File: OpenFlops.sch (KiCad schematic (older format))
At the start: 74 parts, among them P1 FLOPPY_CONN, P2 POWER_INPUT, P3 USB_A_FEMALE, P4 PROG_PORT, P5 JUMPERS, P6 ENCODER_PORT, P7 DISPLAY_PORT, Q1 MOS_N_GSD, Q2 MOS_N_GSD, Q3 MOS_N_GSD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

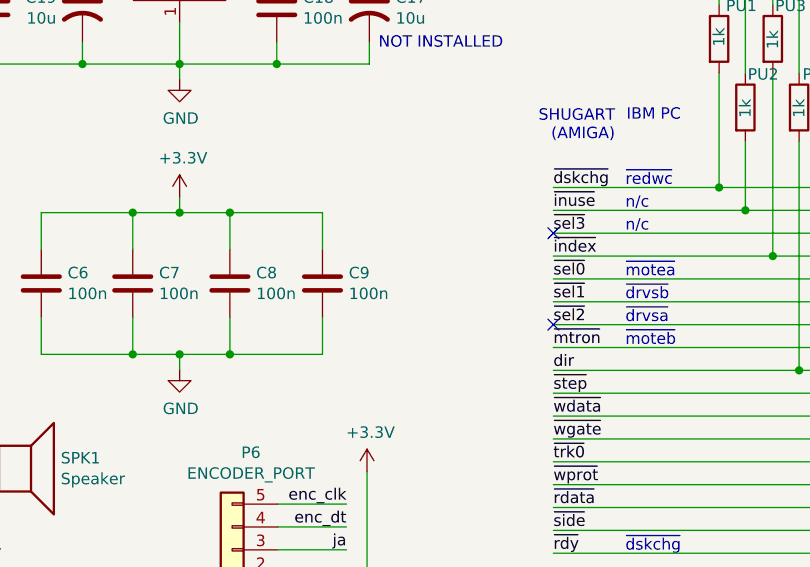
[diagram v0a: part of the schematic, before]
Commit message: Rework power tracks, depolarize OLED/encoder connectors
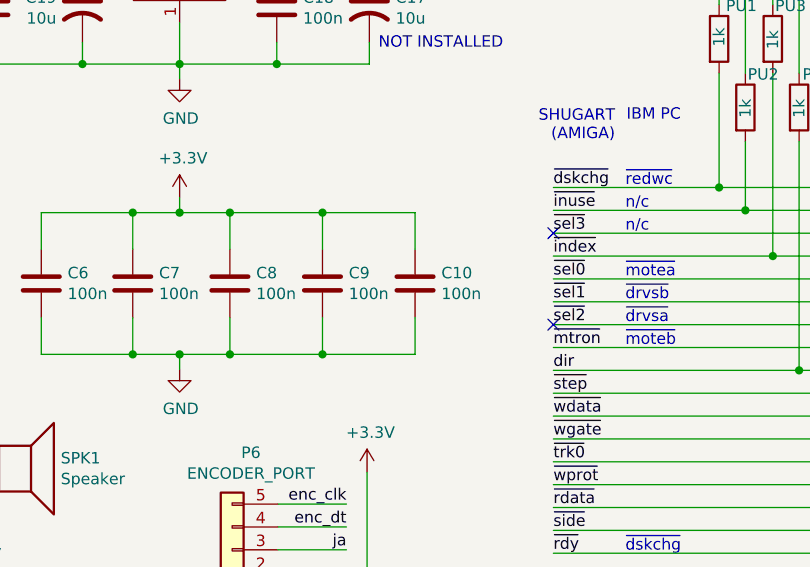
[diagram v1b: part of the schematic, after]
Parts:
- added C10: 100n, Capacitor_SMD:C_0805_2012Metric_Pad1.15x1.40mm_HandSolder, symbol Device:C
- P6: footprint Connector_PinHeader_2.54mm:PinHeader_1x05_P2.54mm_Vertical -> OpenFlops:PinHeader_1x05_P2.54mm_Vertical
- P7: footprint Connector_PinHeader_2.54mm:PinHeader_1x04_P2.54mm_Vertical -> OpenFlops:PinHeader_1x04_P2.54mm_Vertical
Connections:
- net +3V3: now also C10.1
- net GND: now also C10.2
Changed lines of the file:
@@
 Sheet 1 1
 Title "OpenFlops"
-Date "2019-08-04"
+Date "2019-08-14"
 Rev "1git"
 Comp "SukkoPera"
@@
 F 0 "P7" H 7553 4925 50  0000 C CNN
 F 1 "DISPLAY_PORT" H 7553 5016 50  0000 C CNN
-F 2 "Connector_PinHeader_2.54mm:PinHeader_1x04_P2.54mm_Vertical" H 7635 5350 50  0001 C CNN
+F 2 "OpenFlops:PinHeader_1x04_P2.54mm_Vertical" H 7635 5350 50  0001 C CNN
 F 3 "~" H 7635 5350 50  0001 C CNN
 	1    7635 5350
@@
 F 0 "P6" H 6018 4165 50  0000 C CNN
 F 1 "ENCODER_PORT" H 6018 4256 50  0000 C CNN
-F 2 "Connector_PinHeader_2.54mm:PinHeader_1x05_P2.54mm_Vertical" H 6100 4590 50  0001 C CNN
+F 2 "OpenFlops:PinHeader_1x05_P2.54mm_Vertical" H 6100 4590 50  0001 C CNN
 F 3 "~" H 6100 4590 50  0001 C CNN
 	1    6100 4590
@@
 Wire Wire Line
 	4905 4435 4905 4455
+$Comp
+L Device:C C10
+U 1 1 5D58F4BB
+P 6900 3425
+F 0 "C10" H 7015 3471 50  0000 L CNN
+F 1 "100n" H 7015 3380 50  0000 L CNN
+F 2 "Capacitor_SMD:C_0805_2012Metric_Pad1.15x1.40mm_HandSolder" H 6938 3275 50  0001 C CNN
+F 3 "~" H 6900 3425 50  0001 C CNN
+	1    6900 3425
+	1    0    0    -1
+$EndComp
+Wire Wire Line
+	6900 3115 6900 3275
+Wire Wire Line
+	6495 3115 6900 3115
+Wire Wire Line
+	6495 3735 6900 3735
+Wire Wire Line
+	6900 3735 6900 3575
+Connection ~ 6495 3115
+Connection ~ 6495 3735
 $EndSCHEMATC

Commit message: Use SOT-23 footprints for MOSFETs
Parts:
- Q1, Q2, Q3, Q4, Q5, Q6: footprint Package_TO_SOT_SMD:SOT-323_SC-70_Handsoldering -> Package_TO_SOT_SMD:SOT-23_Handsoldering
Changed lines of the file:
@@
 F 0 "Q1" H 3216 5643 70  0000 L CNN
 F 1 "MOS_N_GSD" H 3216 5529 60  0000 L CNN
-F 2 "Package_TO_SOT_SMD:SOT-323_SC-70_Handsoldering" H 3040 5590 60  0001 C CNN
+F 2 "Package_TO_SOT_SMD:SOT-23_Handsoldering" H 3040 5590 60  0001 C CNN
 F 3 "" H 3040 5590 60  0000 C CNN
 	1    3040 5590
@@
 F 0 "Q2" H 3216 6493 70  0000 L CNN
 F 1 "MOS_N_GSD" H 3216 6379 60  0000 L CNN
-F 2 "Package_TO_SOT_SMD:SOT-323_SC-70_Handsoldering" H 3040 6440 60  0001 C CNN
+F 2 "Package_TO_SOT_SMD:SOT-23_Handsoldering" H 3040 6440 60  0001 C CNN
 F 3 "" H 3040 6440 60  0000 C CNN
 	1    3040 6440
@@
 F 0 "Q3" H 3216 7343 70  0000 L CNN
 F 1 "MOS_N_GSD" H 3216 7229 60  0000 L CNN
-F 2 "Package_TO_SOT_SMD:SOT-323_SC-70_Handsoldering" H 3040 7290 60  0001 C CNN
+F 2 "Package_TO_SOT_SMD:SOT-23_Handsoldering" H 3040 7290 60  0001 C CNN
 F 3 "" H 3040 7290 60  0000 C CNN
 	1    3040 7290
@@
 F 0 "Q6" H 5876 7343 70  0000 L CNN
 F 1 "MOS_N_GSD" H 5876 7229 60  0000 L CNN
-F 2 "Package_TO_SOT_SMD:SOT-323_SC-70_Handsoldering" H 5700 7290 60  0001 C CNN
+F 2 "Package_TO_SOT_SMD:SOT-23_Handsoldering" H 5700 7290 60  0001 C CNN
 F 3 "" H 5700 7290 60  0000 C CNN
 	1    5700 7290
@@
 F 0 "Q5" H 5876 6493 70  0000 L CNN
 F 1 "MOS_N_GSD" H 5876 6379 60  0000 L CNN
-F 2 "Package_TO_SOT_SMD:SOT-323_SC-70_Handsoldering" H 5700 6440 60  0001 C CNN
+F 2 "Package_TO_SOT_SMD:SOT-23_Handsoldering" H 5700 6440 60  0001 C CNN
 F 3 "" H 5700 6440 60  0000 C CNN
 	1    5700 6440
@@
 F 0 "Q4" H 5876 5643 70  0000 L CNN
 F 1 "MOS_N_GSD" H 5876 5529 60  0000 L CNN
-F 2 "Package_TO_SOT_SMD:SOT-323_SC-70_Handsoldering" H 5700 5590 60  0001 C CNN
+F 2 "Package_TO_SOT_SMD:SOT-23_Handsoldering" H 5700 5590 60  0001 C CNN
 F 3 "" H 5700 5590 60  0000 C CNN
 	1    5700 5590

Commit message: Use SOD-323 footprint for diodes
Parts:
- D1, D2: footprint Diode_SMD:D_SOD-123 -> Diode_SMD:D_SOD-323_HandSoldering
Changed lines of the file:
@@
 F 0 "D1" H 5375 6561 50  0000 C CNN
 F 1 "1N5819 (?)" H 5375 6470 50  0000 C CNN
-F 2 "Diode_SMD:D_SOD-123" H 5375 6685 50  0001 C CNN
+F 2 "Diode_SMD:D_SOD-323_HandSoldering" H 5375 6685 50  0001 C CNN
 F 3 "~" H 5375 6685 50  0001 C CNN
 	1    5375 6685
@@
 F 0 "D2" V 4674 4324 50  0000 L CNN
 F 1 "1N5819 (?)" V 4765 4324 50  0000 L CNN
-F 2 "Diode_SMD:D_SOD-123" H 4720 4245 50  0001 C CNN
+F 2 "Diode_SMD:D_SOD-323_HandSoldering" H 4720 4245 50  0001 C CNN
 F 3 "~" H 4720 4245 50  0001 C CNN
 	1    4720 4245

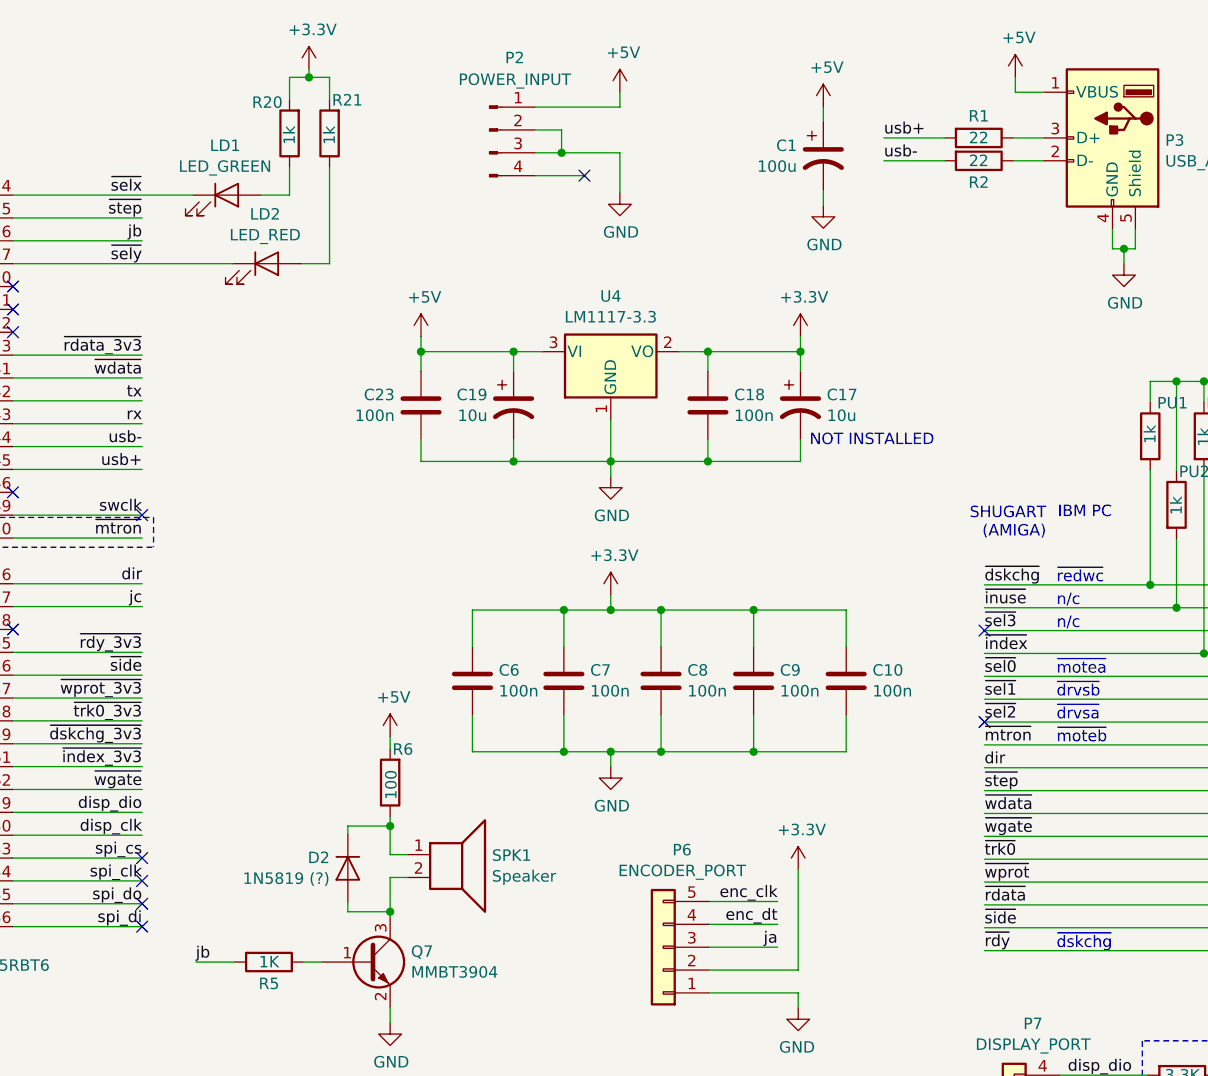
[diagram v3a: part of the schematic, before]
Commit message: Add header for USB and speaker signals - Thanks Ray Bellis
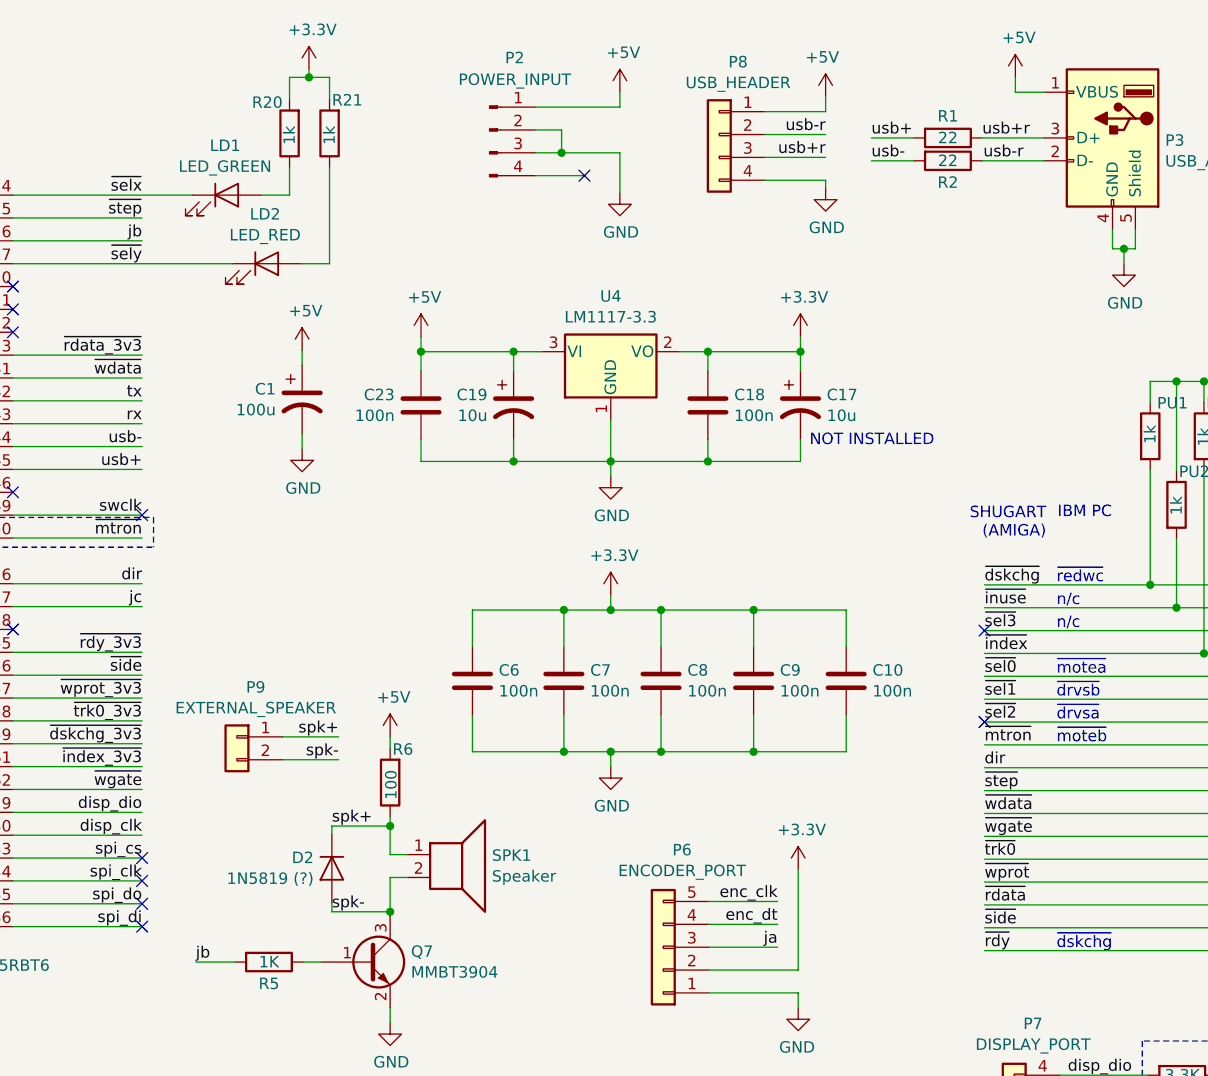
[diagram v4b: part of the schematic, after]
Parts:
- added P8: USB_HEADER, OpenFlops:PinHeader_1x04_P2.54mm_Vertical, symbol Connector_Generic:Conn_01x04
- added P9: EXTERNAL_SPEAKER, OpenFlops:PinHeader_1x02_P2.54mm_Vertical, symbol Connector_Generic:Conn_01x02
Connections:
- net +5V: now also P8.1 (Pin_1)
- net GND: now also P8.4 (Pin_4)
- net spk+: now reaches D2.1 (K), R6.1, SPK1.1
- net spk+: now also P9.1 (Pin_1)
- net spk-: now reaches D2.2 (A), Q7.3 (C), SPK1.2
- net spk-: now also P9.2 (Pin_2)
- net usb-r: now reaches P3.2 (D-), R2.1
- net usb-r: now also P8.2 (Pin_2)
- net usb+r: now reaches P3.3 (D+), R1.1
- net usb+r: now also P8.3 (Pin_3)
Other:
- moved on the sheet: C1, D2, R1, R2
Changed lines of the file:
@@
 Sheet 1 1
 Title "OpenFlops"
-Date "2019-08-14"
+Date "2019-08-18"
 Rev "1git"
 Comp "SukkoPera"
@@
 L Device:R R1
 U 1 1 5D7861B9
-P 7480 1050
-F 0 "R1" V 7385 1050 50  0000 C CNN
-F 1 "22" V 7480 1050 50  0000 C CNN
-F 2 "Resistor_SMD:R_0805_2012Metric_Pad1.15x1.40mm_HandSolder" V 7410 1050 50  0001 C CNN
-F 3 "~" H 7480 1050 50  0001 C CNN
-	1    7480 1050
+P 7345 1050
+F 0 "R1" V 7250 1050 50  0000 C CNN
+F 1 "22" V 7345 1050 50  0000 C CNN
+F 2 "Resistor_SMD:R_0805_2012Metric_Pad1.15x1.40mm_HandSolder" V 7275 1050 50  0001 C CNN
+F 3 "~" H 7345 1050 50  0001 C CNN
+	1    7345 1050
 	0    1    1    0
 $EndComp
@@
 L Device:R R2
 U 1 1 5D786893
-P 7480 1150
-F 0 "R2" V 7575 1150 50  0000 C CNN
-F 1 "22" V 7480 1150 50  0000 C CNN
-F 2 "Resistor_SMD:R_0805_2012Metric_Pad1.15x1.40mm_HandSolder" V 7410 1150 50  0001 C CNN
-F 3 "~" H 7480 1150 50  0001 C CNN
-	1    7480 1150
+P 7345 1150
+F 0 "R2" V 7440 1150 50  0000 C CNN
+F 1 "22" V 7345 1150 50  0000 C CNN
+F 2 "Resistor_SMD:R_0805_2012Metric_Pad1.15x1.40mm_HandSolder" V 7275 1150 50  0001 C CNN
+F 3 "~" H 7345 1150 50  0001 C CNN
+	1    7345 1150
 	0    1    1    0
 $EndComp
 Wire Wire Line
-	7630 1050 7765 1050
-Wire Wire Line
-	7630 1150 7765 1150
-Wire Wire Line
-	7330 1050 7065 1050
-Wire Wire Line
-	7330 1150 7065 1150
-Text Label 7065 1050 0    50   ~ 0
+	7495 1050 7765 1050
+Wire Wire Line
+	7195 1050 7010 1050
+Wire Wire Line
+	7195 1150 7010 1150
+Text Label 7010 1050 0    50   ~ 0
 usb+
-Text Label 7065 1150 0    50   ~ 0
+Text Label 7010 1150 0    50   ~ 0
 usb-
 Wire Wire Line
@@
 L Device:CP1 C1
 U 1 1 5EE6C285
-P 6800 1130
-F 0 "C1" H 6685 1176 50  0000 R CNN
-F 1 "100u" H 6685 1085 50  0000 R CNN
-F 2 "Capacitor_THT:CP_Radial_D6.3mm_P2.50mm" H 6800 1130 50  0001 C CNN
-F 3 "~" H 6800 1130 50  0001 C CNN
-	1    6800 1130
+P 4520 2195
+F 0 "C1" H 4405 2241 50  0000 R CNN
+F 1 "100u" H 4405 2150 50  0000 R CNN
+F 2 "Capacitor_THT:CP_Radial_D6.3mm_P2.50mm" H 4520 2195 50  0001 C CNN
+F 3 "~" H 4520 2195 50  0001 C CNN
+	1    4520 2195
 	1    0    0    -1
 $EndComp
@@
 L power:+5V #PWR0141
 U 1 1 5EE997A6
-P 6800 915
-F 0 "#PWR0141" H 6800 765 50  0001 C CNN
-F 1 "+5V" H 6815 1088 50  0000 C CNN
-F 2 "" H 6800 915 50  0001 C CNN
-F 3 "" H 6800 915 50  0001 C CNN
-	1    6800 915
-	1    0    0    -1
-$EndComp
-Wire Wire Line
-	6800 915  6800 980
+P 4520 1980
+F 0 "#PWR0141" H 4520 1830 50  0001 C CNN
+F 1 "+5V" H 4535 2153 50  0000 C CNN
+F 2 "" H 4520 1980 50  0001 C CNN
+F 3 "" H 4520 1980 50  0001 C CNN
+	1    4520 1980
+	1    0    0    -1
+$EndComp
+Wire Wire Line
+	4520 1980 4520 2045
 $Comp
 L power:GND #PWR0142
 U 1 1 5EEC2A25
-P 6800 1345
-F 0 "#PWR0142" H 6800 1095 50  0001 C CNN
-F 1 "GND" H 6805 1172 50  0000 C CNN
-F 2 "" H 6800 1345 50  0001 C CNN
-F 3 "" H 6800 1345 50  0001 C CNN
-	1    6800 1345
-	1    0    0    -1
-$EndComp
-Wire Wire Line
-	6800 1280 6800 1345
+P 4520 2410
+F 0 "#PWR0142" H 4520 2160 50  0001 C CNN
+F 1 "GND" H 4525 2237 50  0000 C CNN
+F 2 "" H 4520 2410 50  0001 C CNN
+F 3 "" H 4520 2410 50  0001 C CNN
+	1    4520 2410
+	1    0    0    -1
+$EndComp
+Wire Wire Line
+	4520 2345 4520 2410
 Text Label 7505 3305 0    50   ~ 0
 ~index
@@
 	4905 4020 4905 4060
 Wire Wire Line
-	4720 4095 4720 4060
-Wire Wire Line
-	4720 4060 4905 4060
+	4650 4095 4650 4060
+Wire Wire Line
+	4650 4060 4905 4060
 Connection ~ 4905 4060
 Wire Wire Line
 	4905 4060 4905 4185
-Wire Wire Line
-	4720 4395 4720 4435
 $Comp
 L Device:D D2
 U 1 1 5E2F4A52
-P 4720 4245
-F 0 "D2" V 4674 4324 50  0000 L CNN
-F 1 "1N5819 (?)" V 4765 4324 50  0000 L CNN
-F 2 "Diode_SMD:D_SOD-323_HandSoldering" H 4720 4245 50  0001 C CNN
-F 3 "~" H 4720 4245 50  0001 C CNN
-	1    4720 4245
+P 4650 4245
+F 0 "D2" V 4604 4324 50  0000 L CNN
+F 1 "1N5819 (?)" V 4695 4324 50  0000 L CNN
+F 2 "Diode_SMD:D_SOD-323_HandSoldering" H 4650 4245 50  0001 C CNN
+F 3 "~" H 4650 4245 50  0001 C CNN
+	1    4650 4245
 	0    -1   1    0
 $EndComp
@@
 Wire Wire Line
 	4905 4285 4905 4435
-Wire Wire Line
-	4720 4435 4905 4435
 Connection ~ 4905 4435
 Wire Wire Line
@@
 Connection ~ 6495 3115
 Connection ~ 6495 3735
+$Comp
+L Connector_Generic:Conn_01x04 P8
+U 1 1 5D653966
+P 6345 1035
+F 0 "P8" H 6263 1352 50  0000 C CNN
+F 1 "USB_HEADER" H 6263 1261 50  0000 C CNN
+F 2 "OpenFlops:PinHeader_1x04_P2.54mm_Vertical" H 6345 1035 50  0001 C CNN
+F 3 "~" H 6345 1035 50  0001 C CNN
+	1    6345 1035
+	-1   0    0    -1
+$EndComp
+Wire Wire Line
+	6545 1035 6810 1035
+Wire Wire Line
+	6545 1135 6810 1135
+Text Label 6810 1035 2    50   ~ 0
+usb-r
+Text Label 6810 1135 2    50   ~ 0
+usb+r
+$Comp
+L power:+5V #PWR0144
+U 1 1 5D74D3BF
+P 6810 870
+F 0 "#PWR0144" H 6810 720 50  0001 C CNN
+F 1 "+5V" H 6825 1043 50  0000 C CNN
+F 2 "" H 6810 870 50  0001 C CNN
+F 3 "" H 6810 870 50  0001 C CNN
+	1    6810 870
+	-1   0    0    -1
+$EndComp
+Wire Wire Line
+	6810 870  6810 935
+Wire Wire Line
+	6810 935  6545 935
+$Comp
+L power:GND #PWR0145
+U 1 1 5D780CD9
+P 6810 1270
+F 0 "#PWR0145" H 6810 1020 50  0001 C CNN
+F 1 "GND" H 6815 1097 50  0000 C CNN
+F 2 "" H 6810 1270 50  0001 C CNN
+F 3 "" H 6810 1270 50  0001 C CNN
+	1    6810 1270
+	1    0    0    -1
+$EndComp
+Wire Wire Line
+	6545 1235 6810 1235
+Wire Wire Line
+	6810 1235 6810 1270
+$Comp
+L Connector_Generic:Conn_01x02 P9
+U 1 1 5D86073A
+P 4235 3670
+F 0 "P9" H 4153 3887 50  0000 C CNN
+F 1 "EXTERNAL_SPEAKER" H 4153 3796 50  0000 C CNN
+F 2 "OpenFlops:PinHeader_1x02_P2.54mm_Vertical" H 4235 3670 50  0001 C CNN
+F 3 "~" H 4235 3670 50  0001 C CNN
+	1    4235 3670
+	-1   0    0    -1
+$EndComp
+Wire Wire Line
+	4435 3670 4680 3670
+Wire Wire Line
+	4435 3770 4680 3770
+Wire Wire Line
+	4650 4435 4650 4395
+Wire Wire Line
+	4650 4435 4905 4435
+Text Label 4650 4435 0    50   ~ 0
+spk-
+Text Label 4680 3770 2    50   ~ 0
+spk-
+Text Label 4650 4060 0    50   ~ 0
+spk+
+Text Label 4680 3670 2    50   ~ 0
+spk+
+Text Label 7495 1050 0    50   ~ 0
+usb+r
+Text Label 7500 1150 0    50   ~ 0
+usb-r
+Wire Wire Line
+	7495 1150 7765 1150
 $EndSCHEMATC

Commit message: Lotsa cosmetic fixes
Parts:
- removed P5: JUMPERS, Connector_PinHeader_2.54mm:PinHeader_2x07_P2.54mm_Vertical, symbol Connector_Generic:Conn_02x07_Odd_Even
- added P5: JUMPERS, OpenFlops:PinHeader_1x02_P2.54mm_Vertical, symbol Connector_Generic:Conn_01x02
- added PA5, PB5, PC5, PD5: Conn_01x03, OpenFlops:PinHeader_1x03_P2.54mm_Mute, symbol Connector_Generic:Conn_01x03
- P2: footprint Connector_PinHeader_2.54mm:PinHeader_1x04_P2.54mm_Horizontal -> OpenFlops:PinHeader_1x04_P2.54mm_Vertical
- P4: footprint Connector_PinHeader_2.54mm:PinHeader_2x05_P2.54mm_Vertical -> OpenFlops:PinHeader_2x05_P2.54mm_Vertical
- P9: footprint OpenFlops:PinHeader_1x02_P2.54mm_Vertical -> OpenFlops:PinHeader_1x02_P2.54mm_Mute
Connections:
- net +5V: now also PU15.2, PU4.2; no longer PU15.1, PU4.1
- net GND: now also P5.2 (Pin_2)
- net jc: now also P5.1 (Pin_1)
- net ~mtron: now also PD5.2 (Pin_2)
- net ~sel0: now also PA5.2 (Pin_2)
- net ~sel1: now also PB5.2 (Pin_2)
- net ~sel2: now also PC5.2 (Pin_2)
- net ~selx: now also PU4.1, PA5.1 (Pin_1), PB5.1 (Pin_1), PC5.1 (Pin_1), PD5.1 (Pin_1); no longer PU4.2
- net ~sely: now also PU15.1, PA5.3 (Pin_3), PB5.3 (Pin_3), PC5.3 (Pin_3), PD5.3 (Pin_3); no longer PU15.2
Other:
- note removed: "DRV1 - S0"
- note removed: "DRV1 - S1"
- note removed: "DRV2 - S0"
- note removed: "DRV2 - S1"
- note removed: "J5"
- note removed: "JC"
- note removed: "M0"
- moved on the sheet: LD1, LD2, R20, R21

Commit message: Make LQFP-64 footprint easier to handsolder
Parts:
- U3: footprint Package_QFP:LQFP-64_10x10mm_P0.5mm -> OpenFlops:LQFP-64_Handsoldering
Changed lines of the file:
@@
 F 0 "U3" H 3100 4655 50  0000 C CNN
 F 1 "STM32F105RBT6" H 3125 1130 50  0000 C CNN
-F 2 "Package_QFP:LQFP-64_10x10mm_P0.5mm" H 1955 1200 50  0001 R CNN
+F 2 "OpenFlops:LQFP-64_Handsoldering" H 1955 1200 50  0001 R CNN
 F 3 "http://www.st.com/st-web-ui/static/active/en/resource/technical/document/datasheet/CD00220364.pdf" H 2555 2900 50  0001 C CNN
 	1    2555 2900

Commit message: Ready for V1!
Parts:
- added J99: OSHW_LOGO, Symbol:OSHW-Logo2_9.8x8mm_Copper, symbol Connector_Generic:Conn_01x01
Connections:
- no-connect marks 21 -> 22
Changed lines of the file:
@@
 Sheet 1 1
 Title "OpenFlops"
-Date "2019-08-18"
+Date "2019-08-21"
 Rev "1git"
 Comp "SukkoPera"
@@
 Wire Wire Line
 	3965 785  4045 785
+NoConn ~ 10820 6345
+$Comp
+L Connector_Generic:Conn_01x01 J99
+U 1 1 5E184803
+P 11020 6345
+F 0 "J99" H 10880 6465 50  0000 L CNN
+F 1 "OSHW_LOGO" H 10725 6240 50  0000 L CNN
+F 2 "Symbol:OSHW-Logo2_9.8x8mm_Copper" H 11020 6345 50  0001 C CNN
+F 3 "~" H 11020 6345 50  0001 C CNN
+	1    11020 6345
+	1    0    0    -1
+$EndComp
 $EndSCHEMATC

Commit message: Fix #2
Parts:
- renumbered R4 to R3, R3 to R4
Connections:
- net disp_clk: now also U3.29 (PB10); no longer U3.30 (PB11)
- net disp_dio: now also U3.30 (PB11); no longer U3.29 (PB10)
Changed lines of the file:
@@
 Sheet 1 1
 Title "OpenFlops"
-Date "2019-08-21"
+Date "2019-10-09"
 Rev "1git"
 Comp "SukkoPera"
@@
 Wire Wire Line
 	9050 4105 9840 4105
+Text Label 3820 4100 2    50   ~ 0
+disp_dio
 Text Label 3820 4000 2    50   ~ 0
-disp_dio
-Text Label 3820 4100 2    50   ~ 0
 disp_clk
 $Comp
@@
 Wire Wire Line
 	8630 5065 8630 5150
-$Comp
-L Device:R R3
-U 1 1 5D8B343E
-P 8370 5150
-F 0 "R3" V 8325 5315 50  0000 C CNN
-F 1 "3.3K" V 8370 5150 50  0000 C CNN
-F 2 "Resistor_SMD:R_0805_2012Metric_Pad1.15x1.40mm_HandSolder" V 8300 5150 50  0001 C CNN
-F 3 "~" H 8370 5150 50  0001 C CNN
-	1    8370 5150
-	0    1    1    0
-$EndComp
-$Comp
-L Device:R R4
-U 1 1 5D8B4C4A
-P 8370 5250
-F 0 "R4" V 8420 5410 50  0000 C CNN
-F 1 "3.3K" V 8370 5250 50  0000 C CNN
-F 2 "Resistor_SMD:R_0805_2012Metric_Pad1.15x1.40mm_HandSolder" V 8300 5250 50  0001 C CNN
-F 3 "~" H 8370 5250 50  0001 C CNN
-	1    8370 5250
-	0    1    1    0
-$EndComp
 Wire Wire Line
 	7835 5150 8220 5150
@@
 	1    0    0    -1
 $EndComp
+$Comp
+L Device:R R4
+U 1 1 5D8B343E
+P 8370 5150
+F 0 "R4" V 8325 5315 50  0000 C CNN
+F 1 "3.3K" V 8370 5150 50  0000 C CNN
+F 2 "Resistor_SMD:R_0805_2012Metric_Pad1.15x1.40mm_HandSolder" V 8300 5150 50  0001 C CNN
+F 3 "~" H 8370 5150 50  0001 C CNN
+	1    8370 5150
+	0    1    1    0
+$EndComp
+$Comp
+L Device:R R3
+U 1 1 5D8B4C4A
+P 8370 5250
+F 0 "R3" V 8420 5410 50  0000 C CNN
+F 1 "3.3K" V 8370 5250 50  0000 C CNN
+F 2 "Resistor_SMD:R_0805_2012Metric_Pad1.15x1.40mm_HandSolder" V 8300 5250 50  0001 C CNN
+F 3 "~" H 8370 5250 50  0001 C CNN
+	1    8370 5250
+	0    1    1    0
+$EndComp
 $EndSCHEMATC
